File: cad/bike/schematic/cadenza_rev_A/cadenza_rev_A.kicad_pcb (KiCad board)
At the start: 2 copper layers, 90 x 50 mm, 51 parts, among them J2 USB_C_Receptacle, J3 Conn_01x02, J4 Conn_01x02, Q1 BC547, U1 TLC5916, U10 HDSP-A151, U11 TLC5916, U12 HDSP-A151, U13 STM32F105RCTx, U14 INA193, U15 TLC5916, U2 HDSP-A151, U3 TLC5916, U4 HDSP-A151, U5 TLC5916, U6 HDSP-A151, U7 TLC5916, U8 HDSP-A151, U9 TLC5916

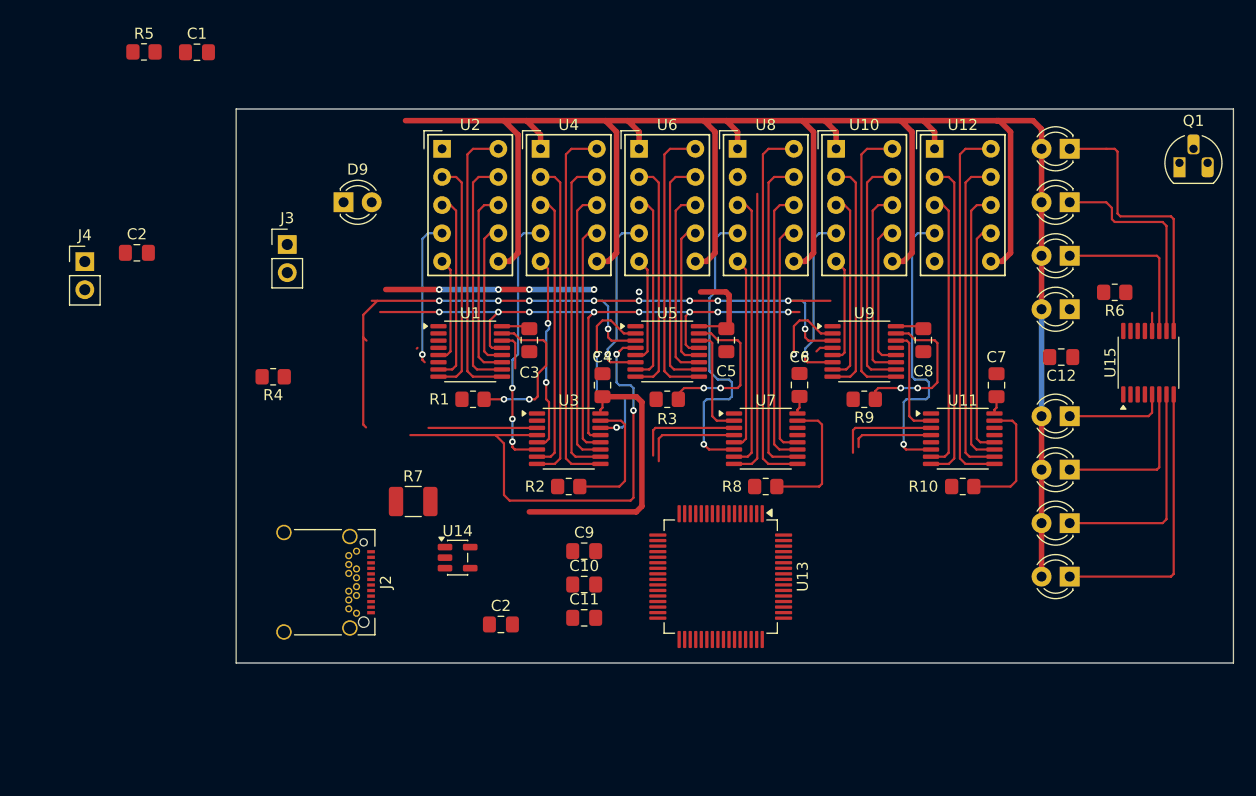
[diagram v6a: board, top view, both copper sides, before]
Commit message: added the 3.3V LDO + switches + push buttons
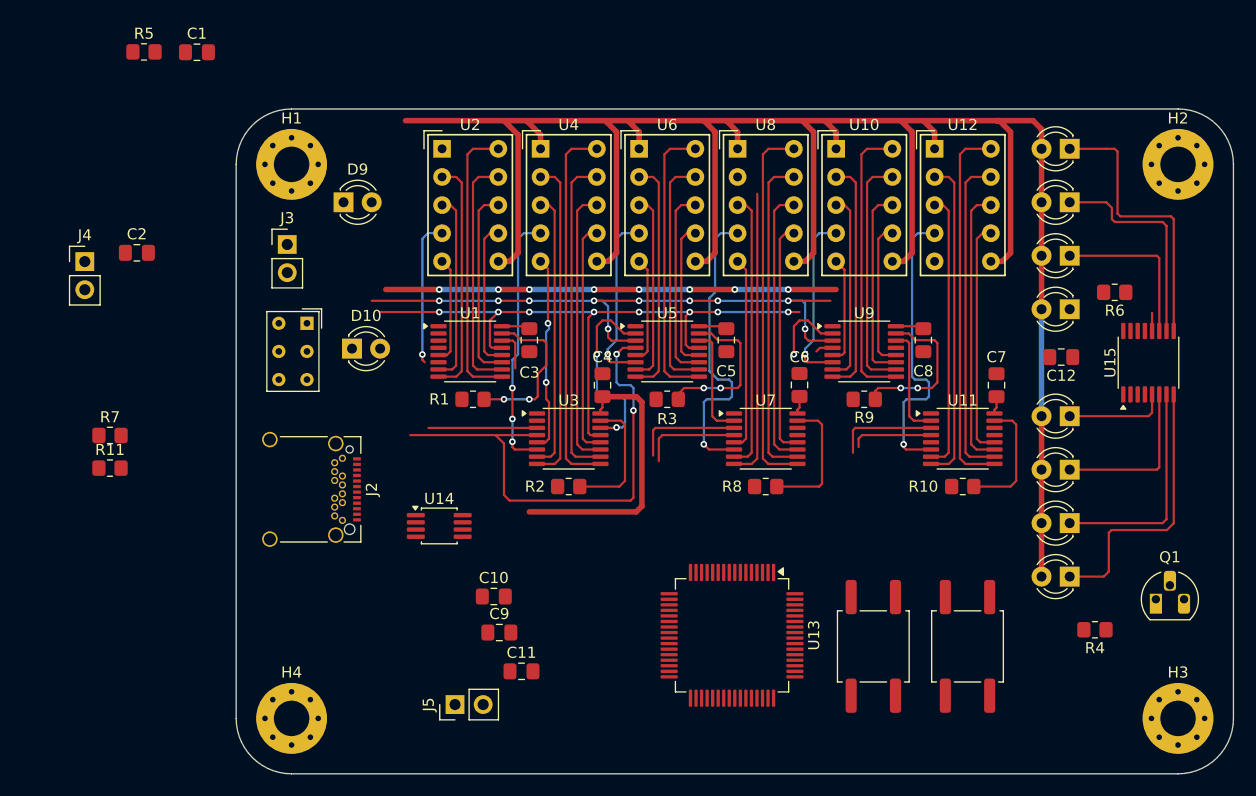
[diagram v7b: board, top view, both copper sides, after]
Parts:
- removed the C2 at (73.9, 96.5)
- added D10: LED, LED_THT:LED_D3.0mm, F.Cu at (60.5, 71.6)
- added H1: MountingHole_Pad, MountingHole:MountingHole_3.2mm_M3_Pad_Via, F.Cu at (55.0, 55.0)
- added H2: MountingHole_Pad, MountingHole:MountingHole_3.2mm_M3_Pad_Via, F.Cu at (135.0, 55.0)
- added H3: MountingHole_Pad, MountingHole:MountingHole_3.2mm_M3_Pad_Via, F.Cu at (135.0, 105.0)
- added H4: MountingHole_Pad, MountingHole:MountingHole_3.2mm_M3_Pad_Via, F.Cu at (55.0, 105.0)
- added J5: Conn_01x02, Connector_PinHeader_2.54mm:PinHeader_1x02_P2.54mm_Vertical, F.Cu at (69.8, 103.8)
- added R11: R_US, Resistor_SMD:R_0805_2012Metric_Pad1.20x1.40mm_HandSolder, F.Cu at (38.6, 82.4)
- added SW1: SW_Slide_DPDT, Button_Switch_THT:SW_NKK_GW12LJP, F.Cu at (56.4, 69.3)
- added SW2: SW_Push, Button_Switch_SMD:SW_Push_1P1T_NO_CK_KSC6xxG, F.Cu at (107.5, 98.5)
- added SW3: SW_Push, Button_Switch_SMD:SW_Push_1P1T_NO_CK_KSC6xxG, F.Cu at (116.0, 98.5)
- R7: value 0.01 -> R_US; footprint Resistor_SMD:R_1210_3225Metric_Pad1.30x2.65mm_HandSolder -> Resistor_SMD:R_0805_2012Metric_Pad1.20x1.40mm_HandSolder
- U14: value INA193 -> LT1962-3.3; footprint Package_TO_SOT_SMD:SOT-23-5 -> Package_SO:MSOP-8_3x3mm_P0.65mm
- moved R4 77.6 mm to (127.5, 97.0)
- moved Q1 39.4 mm to (133.0, 94.2)
- moved R7 28.0 mm to (38.6, 79.5)
- moved C9 10.6 mm to (73.8, 97.2)
- moved J2 8.48 mm to (55.9, 84.3)
- moved C10 8.23 mm to (73.2, 94.0)
- moved C11 7.44 mm to (75.8, 100.8)
- moved U13 5.40 mm to (94.8, 97.5)
- moved U14 3.31 mm to (68.3, 87.6)
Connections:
- J2 pad A4: Net-(J4-Pin_1) -> Net-(J2-VBUS-PadA4)
- J2 pad A9: Net-(J4-Pin_1) -> Net-(J2-VBUS-PadA4)
- J2 pad B4: Net-(J4-Pin_1) -> Net-(J2-VBUS-PadA4)
- J2 pad B9: Net-(J4-Pin_1) -> Net-(J2-VBUS-PadA4)
- J2 pad S1: unconnected-(J2-SHIELD-PadS1) -> GND
- R7 pad 1: Net-(U14-+) -> Net-(J5-Pin_2)
- R7 pad 2: +5V -> GND
- U14 pad 1: unconnected-(U14-Pad1) -> +3.3V
- U14 pad 2: GND -> unconnected-(U14-SENSE-Pad2)
- U14 pad 3: Net-(U14-+) -> unconnected-(U14-BYP-Pad3)
- U14 pad 4: +5V -> GND
- U14 pad 5: +3.3V -> unconnected-(U14-~{SHDN}-Pad5)
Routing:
- net (no net): track 18.8 -> 40.6 mm, vias 4 -> 8
- net /SPI_CLK: track 96.7 -> 84.2 mm
- net +3.3V: track 42.7 -> 37.2 mm, vias 1 -> 0
- net Net-(D8-K): track 25.7 -> 25.1 mm
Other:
- board size 90 x 50 mm -> 90 x 60 mm
